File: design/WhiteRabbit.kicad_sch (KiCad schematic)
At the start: 59 parts

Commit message: new power converter added
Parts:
- C106, C111, C113, C118, C119, C120, C121: renamed from C?; value (none) -> CC0603_22UF_6.3V_20%_X5R; footprint (none) -> CAPC1709X100N
- C107: value (none) -> CC0402_10NF_16V_10%_X7R; footprint (none) -> CAPC1005X55N
- C108, C109, C110, C112, C115, C116, C117, C122, C124, C125, C126, C196, C210, C29, C80, C90, C91: renamed from C?; value (none) -> CC0201_100NF_6.3V_10%_X5R; footprint (none) -> CAPC0603X33N
- C114: value (none) -> CC0402_2.2NF_50V_10%_X7R; footprint (none) -> Capacitors SMD:CAPC1005X55N
- C123, C28, C36, C81: value (none) -> CC0402_1UF_16V_10%_X5R; footprint (none) -> Capacitors SMD:CAPC1005X55N
- C417: value (none) -> CC0402_100NF_25V_10%_X5R; footprint (none) -> Marble:CAPC1005X55N
- L11, L12, L19, L26: renamed from L?; value (none) -> IND0603_MURATA_BLM18SG121TN1D; footprint (none) -> INDC1608X65N
- R100, R101, R102, R82, R94, R96, R97, R98, R99: renamed from R?; value (none) -> R0402_0R_JUMPER; footprint (none) -> RESC1005X40N
- R103: renamed from R?; value (none) -> R0402_100R_1%_0.1W_100PPM; footprint (none) -> RESC1005X40N
- R32: renamed from R?; value (none) -> R0402_10K_1%_0.0625W_100PPM; footprint (none) -> RESC1005X40N
- R58, R92, R93: renamed from R?; value (none) -> R0402_240R_1%_0.0625W_100PPM; footprint (none) -> Resistors SMD:RESC1005X40N
- R79: value (none) -> R0402_40R2_1%_0.0625W_100PPM; footprint (none) -> Resistors SMD:RESC1005X40N
- U13: value (none) -> LP5951MF-3.0/NOPB; footprint (none) -> ICs And Semiconductors SMD:SOT95P284X122-5N
- U14: value (none) -> LM336M-2.5; footprint (none) -> ICs And Semiconductors SMD:SOIC127P600X175-8N
- U16, U19: value (none) -> DAC8550IDGK; footprint (none) -> ICs And Semiconductors SMD:SOP65P490X110-8N
- U20: value (none) -> CDCM61004RHB; footprint (none) -> ICs And Semiconductors SMD:QFN50P500X500X100-33N-S355
- Y1: value (none) -> OSC_25MHZ_RAKON_IVT3205CR; footprint (none) -> ICs And Semiconductors SMD:OSC_ABRACON_ASEMPC
- Y2: value (none) -> VM53S3-25.000-2.5/-30+75; footprint (none) -> ICs And Semiconductors SMD:OSCCC320X500X160-4N
- Y3: value (none) -> OSC_20MHZ_IQD_LFVCXO026156; footprint (none) -> ICs And Semiconductors SMD:OSC_IQD_CFPV-45
- Y6: renamed from OSC?; value (none) -> OSC_10-280MHZ_SILICON-LAB_Si570BBC000121DG; footprint (none) -> ICs And Semiconductors SMD:OSC_SILICON-LAB_SI570

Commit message: fixed parts numners
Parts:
- C417: footprint Marble:CAPC1005X55N -> CAPC1005X55N; ALTIUM_VALUE (none) -> 100nF
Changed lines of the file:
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@@
       (effects (font (size 1.27 1.27)) (justify left) hide)
     )
-    (property "Footprint" "Marble:CAPC1005X55N" (id 2) (at 173.99 48.768 0)
+    (property "Footprint" "CAPC1005X55N" (id 2) (at 173.99 48.768 0)
       (effects (font (size 1.27 1.27)) (justify left) hide)
     )
@@
       (effects (font (size 1.27 1.27)) (justify left) hide)
     )
+    (property "ALTIUM_VALUE" "100nF" (id 39) (at 173.99 40.64 0)
+      (effects (font (size 1.27 1.27)) hide)
+    )
     (pin "1")

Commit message: connected signals to the J9 connector
connected signals to the J9 connector
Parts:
- C106, C107, C108, C109, C110, C111, C112, C113, C114, C115, C116, C117, C118, C119, C120, C121, C122, C123, C124, C125, C126, C196, C210, C28, C29, C36, C417, C80, C81, C90, C91, L11, L12, L19, L26, R100, R101, R102, R103, R32, R58, R79, R82, R92, R93, R94, R96, R97, R98, R99: Author CERN DEM JLC -> (none)
- U16, U19, U20, Y1, Y3, Y6: Author CERN DEM JLC -> (none); Bonding No -> (none)

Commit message: Attempt to add and improve BOM. Added new part numbers for some of the passives
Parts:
- C123, C28, C36, C417, C81, R100, R101, R102, R82, R94, R96, R97, R98, R99: MANUFACTURER (none) -> GENERIC
- R103: MANUFACTURER (none) -> GENERIC; Manufacturer Part Number R0402_100R_1%_0.1W_100PPM_50V -> R0402_100R_1%_0.1W_100PPM
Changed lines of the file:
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@@
     )
     (property "config" "dnf" (id 41) (at 184.15 50.8 0))
+    (property "MANUFACTURER" "GENERIC" (id 42) (at 173.99 52.07 0)
+      (effects (font (size 1.27 1.27)) hide)
+    )
     (pin "1")
     (pin "2")
@@
     )
     (property "config" "dnf" (id 41) (at 184.15 43.18 0))
+    (property "MANUFACTURER" "GENERIC" (id 42) (at 173.99 44.45 0)
+      (effects (font (size 1.27 1.27)) hide)
+    )
     (pin "1")
     (pin "2")
@@
     )
     (property "config" "dnf" (id 41) (at 184.15 45.72 0))
+    (property "MANUFACTURER" "GENERIC" (id 42) (at 173.99 46.99 0)
+      (effects (font (size 1.27 1.27)) hide)
+    )
     (pin "1")
     (pin "2")
@@
     )
     (property "config" "dnf" (id 41) (at 184.15 53.34 0))
+    (property "MANUFACTURER" "GENERIC" (id 42) (at 173.99 54.61 0)
+      (effects (font (size 1.27 1.27)) hide)
+    )
     (pin "1")
     (pin "2")
@@
     )
     (property "config" "dnf" (id 41) (at 184.15 60.96 0))
+    (property "MANUFACTURER" "GENERIC" (id 42) (at 173.99 62.23 0)
+      (effects (font (size 1.27 1.27)) hide)
+    )
     (pin "1")
     (pin "2")
@@
     )
     (property "config" "dnf" (id 41) (at 184.15 63.5 0))
+    (property "MANUFACTURER" "GENERIC" (id 42) (at 173.99 64.77 0)
+      (effects (font (size 1.27 1.27)) hide)
+    )
     (pin "1")
     (pin "2")
@@
       (effects (font (size 1.524 1.524)) (justify left) hide)
     )
+    (property "MANUFACTURER" "GENERIC" (id 40) (at 236.22 69.85 0)
+      (effects (font (size 1.27 1.27)) hide)
+    )
     (pin "1")
     (pin "2")
@@
       (effects (font (size 1.524 1.524)) (justify left) hide)
     )
+    (property "MANUFACTURER" "GENERIC" (id 40) (at 69.85 67.31 0)
+      (effects (font (size 1.27 1.27)) hide)
+    )
     (pin "1")
     (pin "2")
@@
       (effects (font (size 1.524 1.524)) (justify left) hide)
     )
+    (property "MANUFACTURER" "GENERIC" (id 40) (at 17.78 66.04 0)
+      (effects (font (size 1.27 1.27)) hide)
+    )
     (pin "1")
     (pin "2")
@@
       (effects (font (size 1.524 1.524)) (justify left) hide)
     )
+    (property "MANUFACTURER" "GENERIC" (id 41) (at 173.99 57.15 0)
+      (effects (font (size 1.27 1.27)) hide)
+    )
     (pin "1")
     (pin "2")
@@
       (effects (font (size 1.524 1.524)) (justify left) hide)
     )
+    (property "MANUFACTURER" "GENERIC" (id 41) (at 173.99 36.83 0)
+      (effects (font (size 1.27 1.27)) hide)
+    )
     (pin "1")
     (pin "2")
@@
       (effects (font (size 1.524 1.524)) (justify left) hide)
     )
-    (property "Manufacturer Part Number" "R0402_100R_1%_0.1W_100PPM_50V" (id 23) (at 226.06 173.736 0)
+    (property "Manufacturer Part Number" "R0402_100R_1%_0.1W_100PPM" (id 23) (at 226.06 173.736 0)
       (effects (font (size 1.524 1.524)) (justify left) hide)
     )
@@
       (effects (font (size 1.524 1.524)) (justify left) hide)
     )
+    (property "MANUFACTURER" "GENERIC" (id 41) (at 226.06 118.11 0)
+      (effects (font (size 1.27 1.27)) hide)
+    )
     (pin "1")
     (pin "2")
@@
       (effects (font (size 1.524 1.524)) (justify left) hide)
     )
+    (property "MANUFACTURER" "GENERIC" (id 40) (at 186.69 147.32 0)
+      (effects (font (size 1.27 1.27)) hide)
+    )
     (pin "1")
     (pin "2")
@@
       (effects (font (size 1.27 1.27)) hide)
     )
+    (property "MANUFACTURER" "GENERIC" (id 40) (at 173.99 40.64 0)
+      (effects (font (size 1.27 1.27)) hide)
+    )
     (pin "1")
     (pin "2")
@@
       (effects (font (size 1.524 1.524)) (justify left) hide)
     )
+    (property "MANUFACTURER" "GENERIC" (id 41) (at 133.35 45.72 0)
+      (effects (font (size 1.27 1.27)) hide)
+    )
     (pin "1")

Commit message: Restore some consistency in schematic metadata
Still 13 problematic footprint names in LTM4673.kicad_sch:

BAD Dup: "Footprint" "CAPC1608X87N" "Capacitors SMD:CAPC1005X55N" in LTM4673-altium-import:0_Capacitor - non polarized
BAD Dup: "Footprint" "CAPC2012X135N" "CAPC1608X87N" in LTM4673-altium-import:1_Capacitor - non polarized
BAD Dup: "Footprint" "CAPC1608X87N" "Capacitors SMD:CAPC1005X55N" in LTM4673-altium-import:1_Capacitor - non polarized
BAD Dup: "Footprint" "CAPC3216X180N" "CAPC3225X270N" in LTM4673-altium-import:1_Capacitor - non polarized
BAD Dup: "Footprint" "CAPC1608X87N" "Capacitors SMD:CAPC1005X55N" in LTM4673-altium-import:0_Capacitor - non polarized
BAD Dup: "Footprint" "CAPC1608X87N" "Capacitors SMD:CAPC1005X55N" in LTM4673-altium-import:0_Capacitor - non polarized
BAD Dup: "Footprint" "CAPC3216X180N" "CAPC3225X270N" in LTM4673-altium-import:1_Capacitor - non polarized
BAD Dup: "Footprint" "CAPC2012X135N" "CAPC1608X87N" in LTM4673-altium-import:1_Capacitor - non polarized
BAD Dup: "Footprint" "CAPC3216X180N" "CAPC3225X270N" in LTM4673-altium-import:1_Capacitor - non polarized
BAD Dup: "Footprint" "CAPC1608X87N" "Capacitors SMD:CAPC1005X55N" in LTM4673-altium-import:0_Capacitor - non polarized
BAD Dup: "Footprint" "CAPC1608X87N" "Capacitors SMD:CAPC1005X55N" in LTM4673-altium-import:1_Capacitor - non polarized
BAD Dup: "Footprint" "CAPC3216X180N" "CAPC3225X270N" in LTM4673-altium-import:1_Capacitor - non polarized
BAD Dup: "Footprint" "CAPMP7343X310N" "Capacitor_Tantalum_SMD:CP_EIA-7343-30_AVX-N" in LTM4673-altium-import:3_Capacitor - polarized

But the Symbol Field editor in eeschema should be more useful now.
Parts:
- C123, C28, C36, C81, R100, R101, R102, R103, R82, R94, R96, R97, R98, R99: MANUFACTURER GENERIC -> (none)
- C417: ALTIUM_VALUE 100nF -> (none); MANUFACTURER GENERIC -> (none)
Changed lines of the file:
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@@
     )
     (property "config" "dnf" (id 41) (at 184.15 50.8 0))
-    (property "MANUFACTURER" "GENERIC" (id 42) (at 173.99 52.07 0)
-      (effects (font (size 1.27 1.27)) hide)
-    )
     (pin "1")
     (pin "2")
@@
     )
     (property "config" "dnf" (id 41) (at 184.15 43.18 0))
-    (property "MANUFACTURER" "GENERIC" (id 42) (at 173.99 44.45 0)
-      (effects (font (size 1.27 1.27)) hide)
-    )
     (pin "1")
     (pin "2")
@@
     )
     (property "config" "dnf" (id 41) (at 184.15 45.72 0))
-    (property "MANUFACTURER" "GENERIC" (id 42) (at 173.99 46.99 0)
-      (effects (font (size 1.27 1.27)) hide)
-    )
     (pin "1")
     (pin "2")
@@
     )
     (property "config" "dnf" (id 41) (at 184.15 53.34 0))
-    (property "MANUFACTURER" "GENERIC" (id 42) (at 173.99 54.61 0)
-      (effects (font (size 1.27 1.27)) hide)
-    )
     (pin "1")
     (pin "2")
@@
     )
     (property "config" "dnf" (id 41) (at 184.15 60.96 0))
-    (property "MANUFACTURER" "GENERIC" (id 42) (at 173.99 62.23 0)
-      (effects (font (size 1.27 1.27)) hide)
-    )
     (pin "1")
     (pin "2")
@@
     )
     (property "config" "dnf" (id 41) (at 184.15 63.5 0))
-    (property "MANUFACTURER" "GENERIC" (id 42) (at 173.99 64.77 0)
-      (effects (font (size 1.27 1.27)) hide)
-    )
     (pin "1")
     (pin "2")
@@
       (effects (font (size 1.524 1.524)) (justify left) hide)
     )
-    (property "MANUFACTURER" "GENERIC" (id 40) (at 236.22 69.85 0)
-      (effects (font (size 1.27 1.27)) hide)
-    )
     (pin "1")
     (pin "2")
@@
       (effects (font (size 1.524 1.524)) (justify left) hide)
     )
-    (property "MANUFACTURER" "GENERIC" (id 40) (at 69.85 67.31 0)
-      (effects (font (size 1.27 1.27)) hide)
-    )
     (pin "1")
     (pin "2")
@@
       (effects (font (size 1.524 1.524)) (justify left) hide)
     )
-    (property "MANUFACTURER" "GENERIC" (id 40) (at 17.78 66.04 0)
-      (effects (font (size 1.27 1.27)) hide)
-    )
     (pin "1")
     (pin "2")
@@
       (effects (font (size 1.524 1.524)) (justify left) hide)
     )
-    (property "MANUFACTURER" "GENERIC" (id 41) (at 173.99 57.15 0)
-      (effects (font (size 1.27 1.27)) hide)
-    )
     (pin "1")
     (pin "2")
@@
       (effects (font (size 1.524 1.524)) (justify left) hide)
     )
-    (property "MANUFACTURER" "GENERIC" (id 41) (at 173.99 36.83 0)
-      (effects (font (size 1.27 1.27)) hide)
-    )
     (pin "1")
     (pin "2")
@@
       (effects (font (size 1.524 1.524)) (justify left) hide)
     )
-    (property "MANUFACTURER" "GENERIC" (id 41) (at 226.06 118.11 0)
-      (effects (font (size 1.27 1.27)) hide)
-    )
     (pin "1")
     (pin "2")
@@
       (effects (font (size 1.524 1.524)) (justify left) hide)
     )
-    (property "MANUFACTURER" "GENERIC" (id 40) (at 186.69 147.32 0)
-      (effects (font (size 1.27 1.27)) hide)
-    )
     (pin "1")
     (pin "2")
@@
       (effects (font (size 1.27 1.27)) (justify left) hide)
     )
-    (property "ALTIUM_VALUE" "100nF" (id 39) (at 173.99 40.64 0)
-      (effects (font (size 1.27 1.27)) hide)
-    )
-    (property "MANUFACTURER" "GENERIC" (id 40) (at 173.99 40.64 0)
-      (effects (font (size 1.27 1.27)) hide)
-    )
     (pin "1")
     (pin "2")
@@
       (effects (font (size 1.524 1.524)) (justify left) hide)
     )
-    (property "MANUFACTURER" "GENERIC" (id 41) (at 133.35 45.72 0)
-      (effects (font (size 1.27 1.27)) hide)
-    )
     (pin "1")

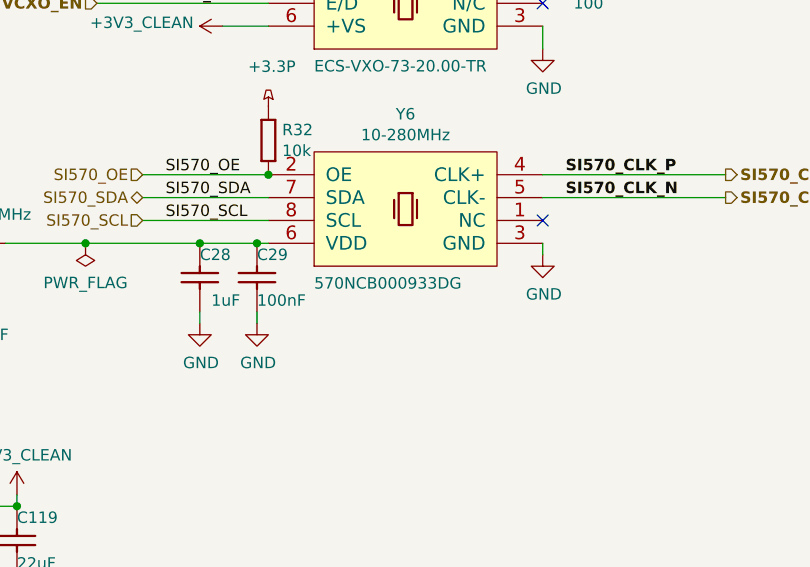
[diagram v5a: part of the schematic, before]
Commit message: new PN for Si570, PCB routing
new PN for Si570, PCB routing
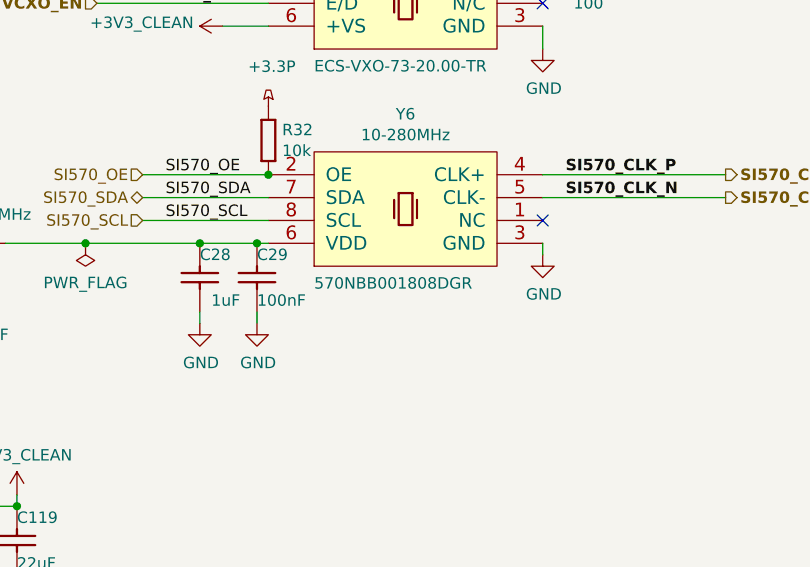
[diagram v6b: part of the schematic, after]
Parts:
- Y6: value OSC_10-280MHZ_SILICON-LAB_Si570BBC000121DG -> OSC_10-280MHZ_SILICON-LAB_570NBB001808DGR; Manufacturer Part Number 570NCB000933DG -> 570NBB001808DGR; Part Number OSC_10-280MHZ_SILICON-LAB_Si570BBC000121DG -> OSC_10-280MHZ_SILICON-LAB_570NBB001808DGR
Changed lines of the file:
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@@
     (in_bom yes) (on_board yes)
     (property "Reference" "Y6" (id 0) (at 209.55 132.969 0))
-    (property "Value" "OSC_10-280MHZ_SILICON-LAB_Si570BBC000121DG" (id 1) (at 199.39 154.305 0)
+    (property "Value" "OSC_10-280MHZ_SILICON-LAB_570NBB001808DGR" (id 1) (at 199.39 154.305 0)
       (effects (font (size 1.27 1.27)) (justify left) hide)
     )
@@
     )
     (property "Val" "10-280MHz" (id 4) (at 209.55 135.2804 0))
-    (property "Part Number" "OSC_10-280MHZ_SILICON-LAB_Si570BBC000121DG" (id 5) (at 199.39 160.02 0)
+    (property "Part Number" "OSC_10-280MHZ_SILICON-LAB_570NBB001808DGR" (id 5) (at 199.39 160.02 0)
       (effects (font (size 1.27 1.27)) (justify left) hide)
     )
@@
       (effects (font (size 1.27 1.27)) (justify left) hide)
     )
-    (property "Manufacturer Part Number" "570NCB000933DG" (id 16) (at 199.39 151.765 0)
+    (property "Manufacturer Part Number" "570NBB001808DGR" (id 16) (at 199.39 151.765 0)
       (effects (font (size 1.27 1.27)) (justify left))
     )
